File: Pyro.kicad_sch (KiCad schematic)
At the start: 9 parts, among them J3 Conn_01x02_Male, Q1 BUK9M11-40EX, U6 LTV-247

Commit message: update
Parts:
- renumbered D3 to D4, D5 to D6, J3 to J10, Q1 to Q2, R18 to R65, R20 to R68, R22 to R70, U6 to U7
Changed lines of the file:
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@@
   (symbol (lib_id "Connector:Conn_01x02_Male") (at 70.358 27.686 90) (mirror x) (unit 1)
     (in_bom yes) (on_board yes) (dnp no)
-    (property "Reference" "J3" (at 69.5198 27.4863 90)
+    (property "Reference" "J10" (at 69.5198 27.4863 90)
       (effects (font (size 1.27 1.27)) (justify left))
     )
@@
   (symbol (lib_id "Device:LED") (at 103.378 67.056 90) (unit 1)
     (in_bom yes) (on_board yes) (dnp no) (fields_autoplaced)
-    (property "Reference" "D5" (at 107.188 68.0085 90)
+    (property "Reference" "D6" (at 107.188 68.0085 90)
       (effects (font (size 1.27 1.27)) (justify right))
     )
@@
   (symbol (lib_id "Device:R") (at 118.618 68.326 0) (unit 1)
     (in_bom yes) (on_board yes) (dnp no) (fields_autoplaced)
-    (property "Reference" "R22" (at 120.396 67.4913 0)
+    (property "Reference" "R70" (at 120.396 67.4913 0)
       (effects (font (size 1.27 1.27)) (justify left))
     )
@@
   (symbol (lib_id "Device:R") (at 47.498 77.216 0) (unit 1)
     (in_bom yes) (on_board yes) (dnp no) (fields_autoplaced)
-    (property "Reference" "R18" (at 50.038 75.9459 0)
+    (property "Reference" "R65" (at 50.038 75.9459 0)
       (effects (font (size 1.27 1.27)) (justify left))
     )
@@
   (symbol (lib_id "power:+3V3") (at 98.298 50.546 0) (unit 1)
     (in_bom yes) (on_board yes) (dnp no) (fields_autoplaced)
-    (property "Reference" "#PWR054" (at 98.298 54.356 0)
+    (property "Reference" "#PWR0133" (at 98.298 54.356 0)
       (effects (font (size 1.27 1.27)) hide)
     )
@@
   (symbol (lib_id "Device:D_Schottky_AAK") (at 80.518 48.006 90) (unit 1)
     (in_bom yes) (on_board yes) (dnp no) (fields_autoplaced)
-    (property "Reference" "D3" (at 83.058 46.482 90)
+    (property "Reference" "D4" (at 83.058 46.482 90)
       (effects (font (size 1.27 1.27)) (justify right))
     )
@@
   (symbol (lib_id "Device:R") (at 103.378 59.436 0) (unit 1)
     (in_bom yes) (on_board yes) (dnp no) (fields_autoplaced)
-    (property "Reference" "R20" (at 105.918 58.1659 0)
+    (property "Reference" "R68" (at 105.918 58.1659 0)
       (effects (font (size 1.27 1.27)) (justify left))
     )
@@
   (symbol (lib_id "power:GND") (at 72.898 78.486 0) (unit 1)
     (in_bom yes) (on_board yes) (dnp no) (fields_autoplaced)
-    (property "Reference" "#PWR052" (at 72.898 84.836 0)
+    (property "Reference" "#PWR083" (at 72.898 84.836 0)
       (effects (font (size 1.27 1.27)) hide)
     )
@@
   (symbol (lib_id "Isolator:LTV-247") (at 110.998 53.086 0) (mirror y) (unit 1)
     (in_bom yes) (on_board yes) (dnp no) (fields_autoplaced)
-    (property "Reference" "U6" (at 110.998 45.466 0)
-      (effects (font (size 1.27 1.27)))
-    )
-    (property "Value" "LTV-247" (at 110.998 48.006 0)
+    (property "Reference" "U7" (at 110.998 44.45 0)
+      (effects (font (size 1.27 1.27)))
+    )
+    (property "Value" "LTV-247" (at 110.998 46.99 0)
       (effects (font (size 1.27 1.27)))
     )
@@
   (symbol (lib_id "power:GND") (at 47.498 81.026 0) (unit 1)
     (in_bom yes) (on_board yes) (dnp no)
-    (property "Reference" "#PWR017" (at 47.498 87.376 0)
+    (property "Reference" "#PWR081" (at 47.498 87.376 0)
       (effects (font (size 1.27 1.27)) hide)
     )
@@
   (symbol (lib_id "Transistor_FET:BUK9M11-40EX") (at 70.358 68.326 0) (unit 1)
     (in_bom yes) (on_board yes) (dnp no) (fields_autoplaced)
-    (property "Reference" "Q1" (at 76.708 67.691 0)
+    (property "Reference" "Q2" (at 76.708 67.691 0)
       (effects (font (size 1.27 1.27)) (justify left))
     )
@@
   (symbol (lib_id "power:GND") (at 110.998 78.486 0) (unit 1)
     (in_bom yes) (on_board yes) (dnp no) (fields_autoplaced)
-    (property "Reference" "#PWR056" (at 110.998 84.836 0)
-      (effects (font (size 1.27 1.27)) hide)
-    )
+    (property "Reference" "#PWR0135" (at 110.998 84.836 0)
+      (effects (font (size 1.27 1.27)) hide)
+    )

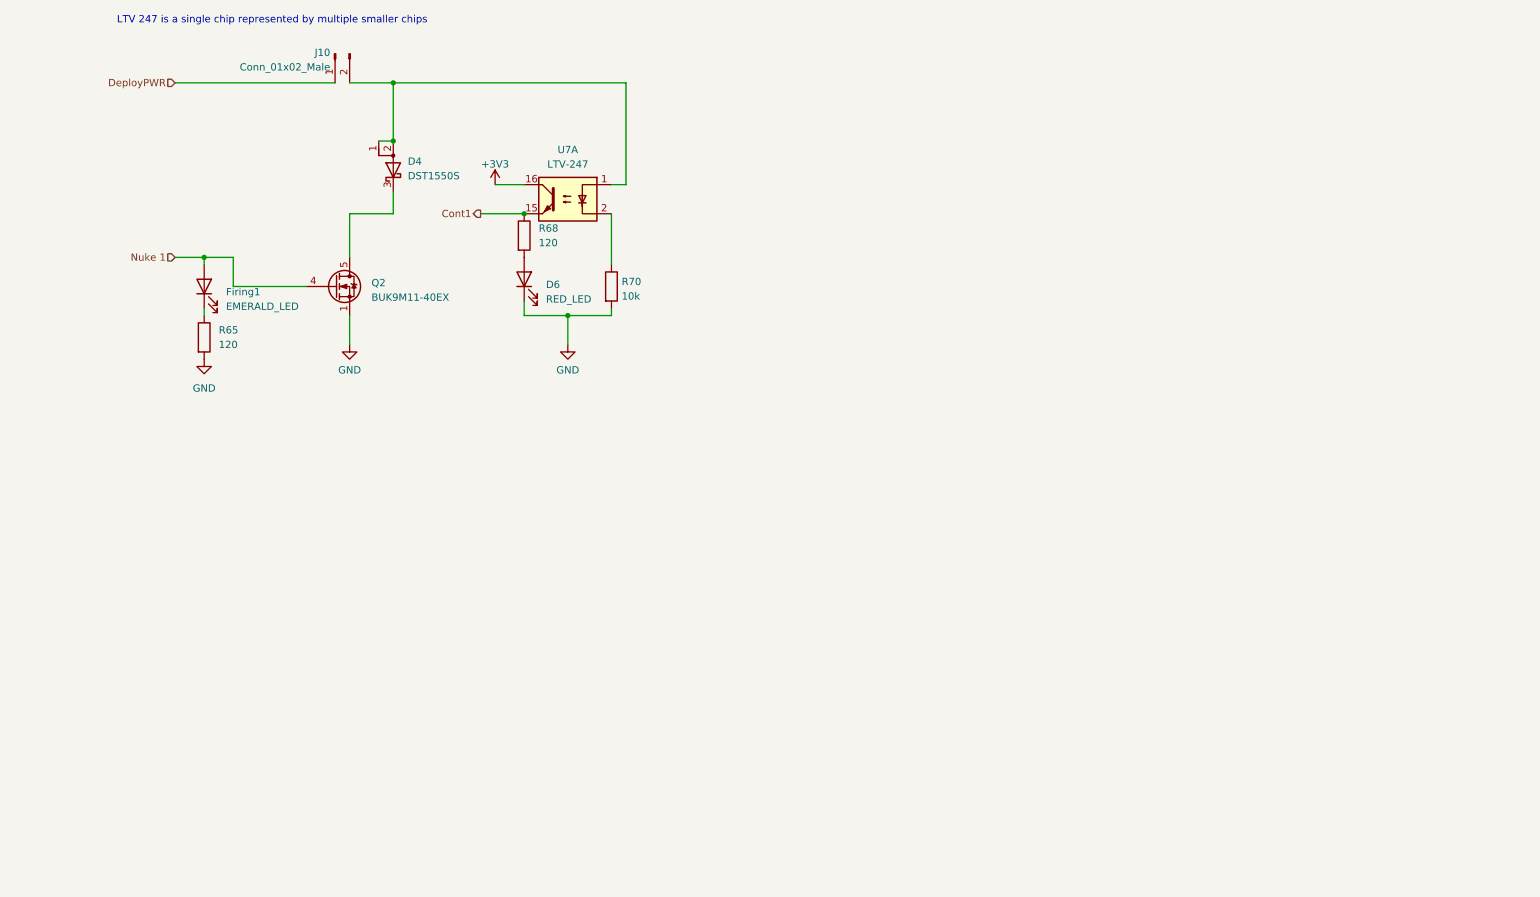
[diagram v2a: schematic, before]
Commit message: Schematic done, components layed out, sensors wired up
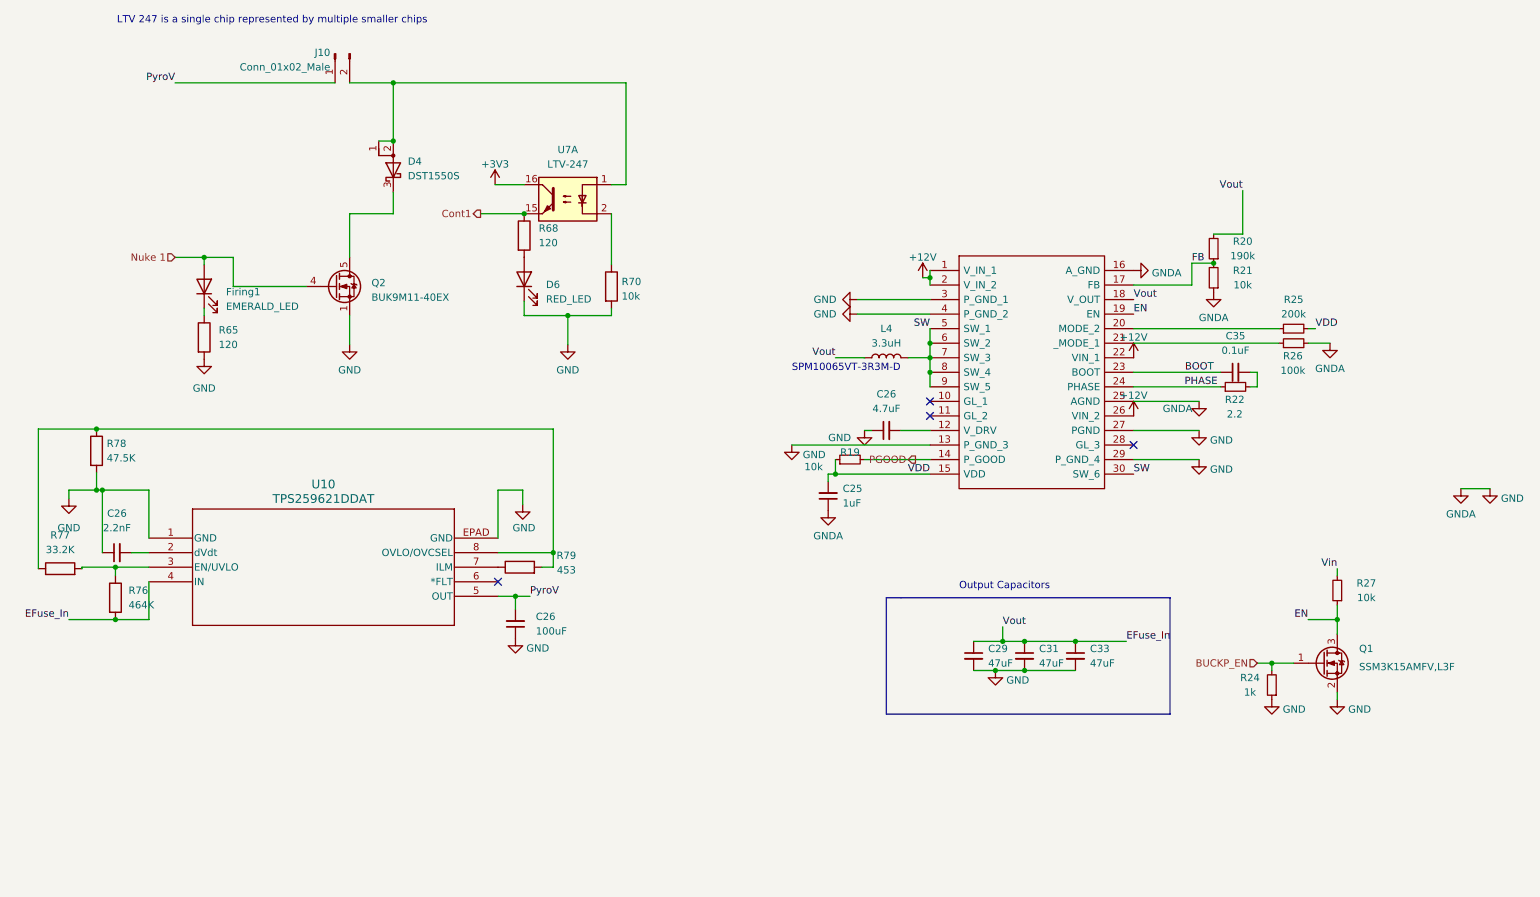
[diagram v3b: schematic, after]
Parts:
- added C25: 1uF, Capacitor_SMD:C_0402_1005Metric, symbol Device:C_Small
- added C26: 2.2nF, Capacitor_SMD:C_0402_1005Metric, symbol Device:C_Small
- added C26: 4.7uF, Capacitor_SMD:C_0402_1005Metric, symbol Device:C_Small
- added C26: 100uF, Capacitor_SMD:C_0402_1005Metric, symbol Device:C_Small
- added C29, C31, C33: 47uF, Capacitor_SMD:C_1206_3216Metric, symbol Device:C_Small
- added C35: 0.1uF, Capacitor_SMD:C_0402_1005Metric, symbol Device:C_Small
- added L4: 3.3uH, iclr:IND_SRP6540-390M, symbol Device:L
- added Q1: SSM3K15AMFV,L3F, Package_TO_SOT_SMD:SOT-723, symbol Device:Q_NMOS_GSD
- added R19, R21, R27: 10k, Resistor_SMD:R_0402_1005Metric, symbol Device:R_Small
- added R20: 190k, Resistor_SMD:R_0402_1005Metric, symbol Device:R_Small
- added R22: 2.2, Resistor_SMD:R_0402_1005Metric, symbol Device:R_Small
- added R24: 1k, Resistor_SMD:R_0402_1005Metric, symbol Device:R_Small
- added R25: 200k, Resistor_SMD:R_0402_1005Metric, symbol Device:R_Small
- added R26: 100k, Resistor_SMD:R_0402_1005Metric, symbol Device:R_Small
- added R76: 464K, Resistor_SMD:R_0402_1005Metric, symbol Device:R
- added R77: 33.2K, Resistor_SMD:R_0402_1005Metric, symbol Device:R
- added R78: 47.5K, Resistor_SMD:R_0402_1005Metric, symbol Device:R
- added R79: 453, Resistor_SMD:R_0402_1005Metric, symbol Device:R
- added U10: TPS259621DDAT, EFuse:SO-PP-DDA-8_TEX, symbol EFuse:TPS259621DDAT
- added U6: SiC437BED-T1-GE3, iclr:SiC437BEDT1GE3, symbol iclr:SiC437BED-T1-GE3
- U7: footprint Package_SO:SOP-16_4.4x10.4mm_P1.27mm -> Package_DIP:SMDIP-4_W9.53mm
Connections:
- net GND: now also C25.1, C26.1, C26.1, C26.1, C29.2, C31.2, C33.2, Q1.2 (S), R21.1, R24.1, R26.2, R78.2, U10.1 (GND), U10.EPAD (GND), U6.13 (P_GND_3), U6.16 (A_GND), U6.25 (AGND), U6.27 (PGND), U6.29 (P_GND_4), U6.3 (P_GND_1), U6.4 (P_GND_2)
- net DeployPWR renamed PyroV
- net PyroV: now also C26.2, U10.5 (OUT)
- new net: R25.1, U6.20 (MODE_2)
- new net: C26.2, U10.2 (dVdt)
- new net: R76.1, R77.2, U10.3 (EN/UVLO)
- new net: R79.1, U10.7 (ILM)
- new net: R77.1, R78.1, R79.2, U10.8 (OVLO/OVCSEL)
- new net: C35.2, R22.2
- new net: C26.2, U6.12 (V_DRV)
- new net: R26.1, U6.21 (_MODE_1)
- new net +12V: U6.1 (V_IN_1), U6.2 (V_IN_2), U6.22 (VIN_1), U6.26 (VIN_2)
- new net BOOT: C35.1, U6.23 (BOOT)
- new net BUCKP_EN: Q1.1 (G), R24.2
- new net EFuse_In: C29.1, C31.1, C33.1, L4.1, R20.2, R76.2, U10.4 (IN), U6.18 (V_OUT)
- new net EN: Q1.3 (D), R27.1, U6.19 (EN)
- new net FB: R20.1, R21.2, U6.17 (FB)
- new net PGOOD: R19.2, U6.14 (P_GOOD)
- new net PHASE: R22.1, U6.24 (PHASE)
- new net SW: L4.2, U6.30 (SW_6), U6.5 (SW_1), U6.6 (SW_2), U6.7 (SW_3), U6.8 (SW_4), U6.9 (SW_5)
- new net VDD: C25.2, R19.1, R25.2, U6.15 (VDD)
- new net Vin: R27.2
- no-connect marks 0 -> 4
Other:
- note added: "Output Capacitors"
- note added: "SPM10065VT-3R3M-D"

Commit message: v1.2
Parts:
- removed C29, C31: 47uF, Capacitor_SMD:C_1206_3216Metric, symbol Device:C_Small
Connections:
- net EFuse_In is gone; now on net GND: C33.1, L4.1, R20.2, R76.2, U10.4 (IN), U6.18 (V_OUT)
- net Vin is gone; now on net +12V: R27.2

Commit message: More Based
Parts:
- renumbered D4 to D3, D6 to D4, J10 to J12, R77 to R74, R78 to R75, R65 to R77, R79 to R78, R68 to R79, R70 to R80, U10 to U8, U7 to U9

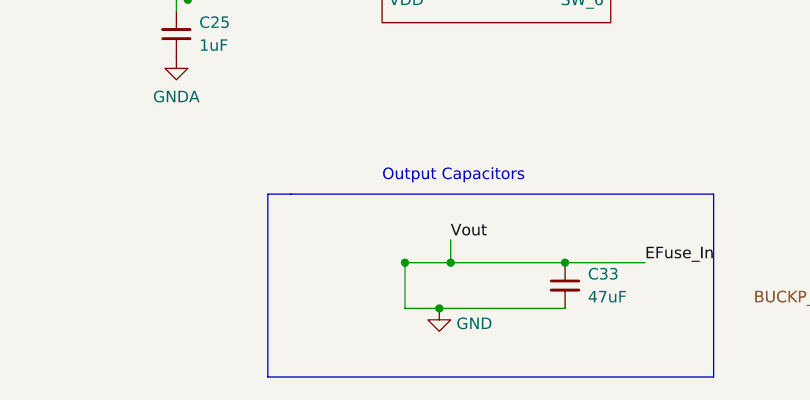
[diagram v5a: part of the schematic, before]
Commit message: Lol pyro buck out  was shorting straight to ground
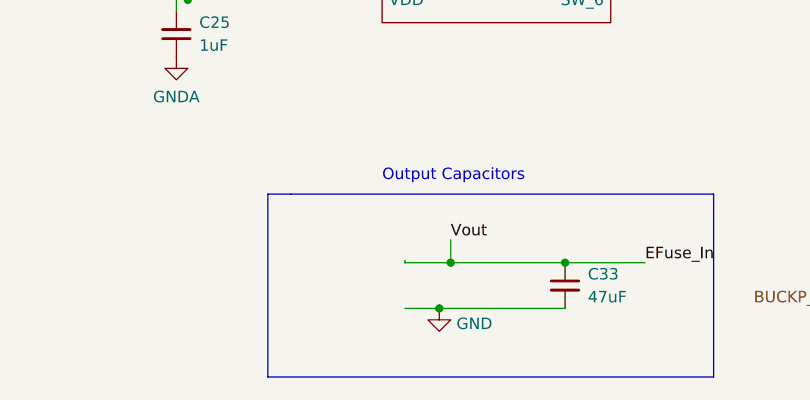
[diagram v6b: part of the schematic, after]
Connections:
- net GND: no longer C33.1, L4.1, R20.2, R76.2, U6.18 (V_OUT), U8.4 (IN)
- new net EFuse_In: C33.1, L4.1, R20.2, R76.2, U6.18 (V_OUT), U8.4 (IN)
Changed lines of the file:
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@@
   (junction (at 80.518 32.766) (diameter 0) (color 0 0 0 0)
-  )
-  (junction (at 181.864 130.302) (diameter 0) (color 0 0 0 0)
   )
   (junction (at 185.674 135.382) (diameter 0) (color 0 0 0 0)
@@
     (stroke (width 0) (type default))
   )
-  (wire (pts (xy 181.864 130.302) (xy 181.864 135.382))
-    (stroke (width 0) (type default))
-  )
